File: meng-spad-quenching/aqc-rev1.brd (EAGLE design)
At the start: 127 x 88.9 mm, 137 parts, among them IC1 ADCMP582, IC2 NC7SV74K8X, IC3 LT3032-5, IC4 OPA342, IC5 OPA342, IC6 LTC1711, IC7 DS1100LU-20+, IC8 LT3032-15, IC9 NC7WZ16P6X, J1 VIN_LOGIC, M1 BSS806N, Q1 MMBTH81, Q2 MMBTH81, Q3 MMBTH81, Q4 MMBTH81, Q5 MMBTH81, Q6 MMBTH81, T1 MMBTH10, T2 MMBTH10, T3 MMBTH10, T4 MMBTH10, T5 MMBTH10, T6 MMBTH10, T7 MMBTH10, U1 SN65EPT21DGK, U2 TPS78233DDCT, U3 SN65EPT22DGK, X1 CONN_SPAD, X2 CONN_PHOTON_COUNTER, X3 CONN_FORCE_QUENCH, X4 CONN_VREF_ONE_SHOT_EXT, X5 CONN_VREF_DIAMOND_IBIAS_EXT, X6 CONN_VREF_CASCODE_IBIAS_EXT

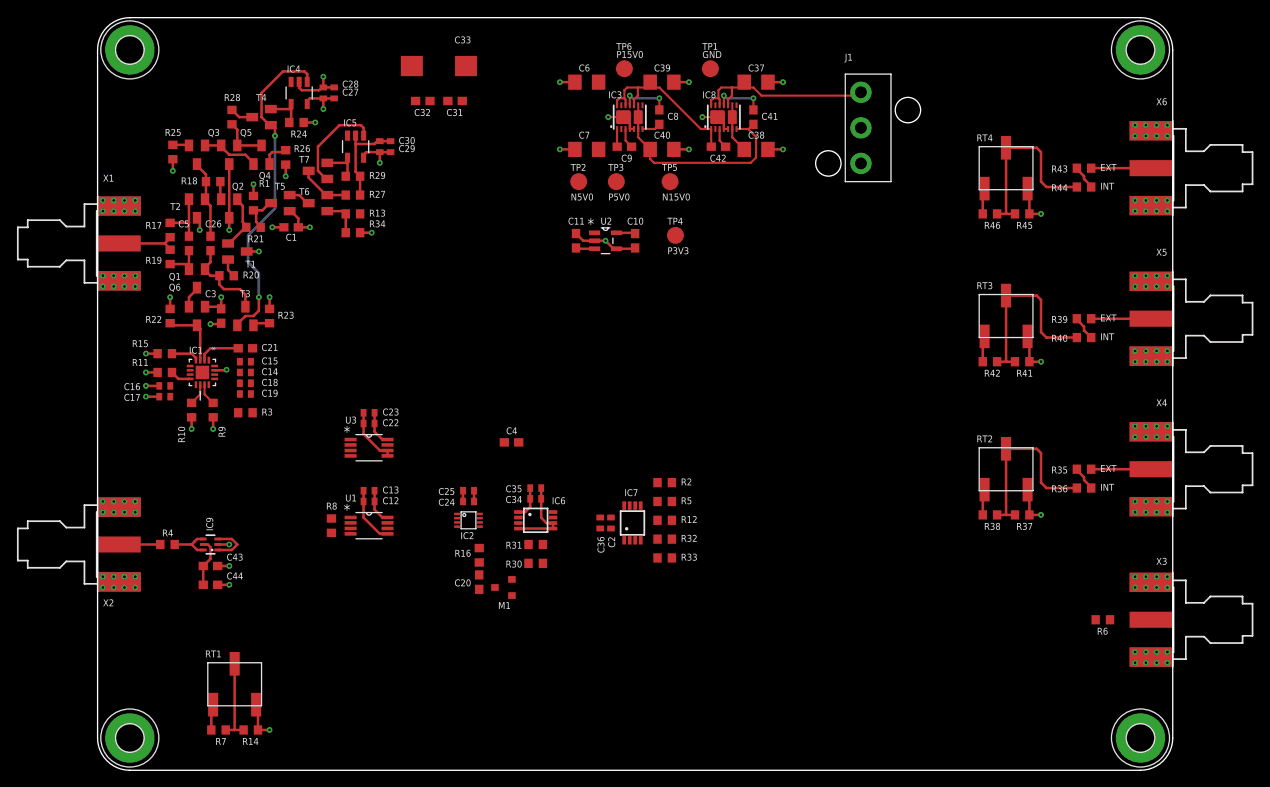
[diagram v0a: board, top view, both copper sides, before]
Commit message: More layout, switched delay line to be driven from line driver
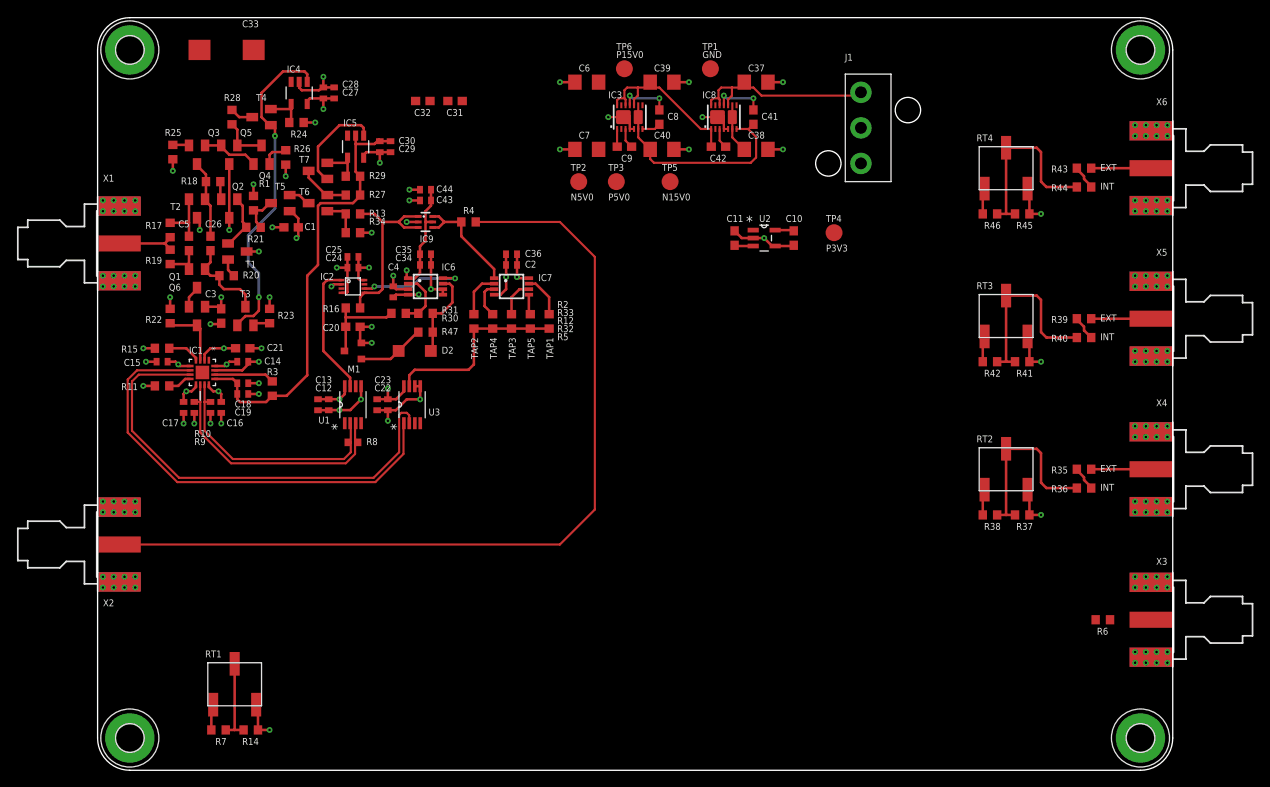
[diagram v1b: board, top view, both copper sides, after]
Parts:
- added D2: SD101BW-TP, diode:SOD123
- added R47: 49R9, rcl:R0603
- C4, C43, C44: device rcl:C0603 -> rcl:C0402
- R10, R8, R9: device rcl:R0603 -> rcl:R0402
- moved C44 53.1 mm to (38.7, 68.6), turned to 180 degrees
- moved R4 52.1 mm to (43.8, 64.8), turned to 180 degrees
- moved C43 50.1 mm to (38.7, 67.3), turned to 180 degrees
- moved IC9 45.8 mm to (38.7, 64.8), turned to 270 degrees
- moved R30 33.7 mm to (35.6, 54.0), turned to 180 degrees
- moved C20 33.7 mm to (30.2, 52.4), turned to 0 degrees
- moved C36 33.4 mm to (48.9, 61.0), turned to 180 degrees
- moved M1 33.1 mm to (30.2, 49.5)
- moved R16 32.8 mm to (30.2, 54.6), turned to 0 degrees
- moved R32 32.8 mm to (46.7, 53.0), turned to 90 degrees
- moved C2 32.7 mm to (48.9, 59.7), turned to 180 degrees
- moved R33 32.1 mm to (51.1, 53.0), turned to 90 degrees
- moved IC7 31.4 mm to (48.9, 57.1), turned to 270 degrees
- moved R5 31.0 mm to (44.5, 53.0), turned to 90 degrees
- moved IC2 30.8 mm to (30.2, 57.1)
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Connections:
- new net N$36: D2.C, M1.1, R47.2
- net LOGIC_QUENCH: no longer IC7.1
- net N$37: now also IC7.1
- net ONE_SHOT_CLR: now also D2.A, R47.1; no longer M1.1
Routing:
- net N$2: track 4.84 -> 103.5 mm
- net PP_P3V3: track 27.6 -> 92.6 mm, vias 0 -> 8
- net COMP_LE_P: track 0.00 -> 54.9 mm
- net COMP_LE_N: track 0.00 -> 54.1 mm
- net PP_N5V0: track 13.9 -> 54.5 mm
- net PP_P5V0: track 22.6 -> 58.8 mm, vias 3 -> 5
- net COMP_Q_N: track 2.57 -> 30.7 mm
- net COMP_Q_P: track 2.57 -> 29.0 mm
- net GND: track 132.9 -> 158.9 mm, vias 128 -> 142
- net BLANKING_LATCH_EN: track 0.00 -> 22.6 mm
- net LOGIC_QUENCH: track 5.19 -> 22.4 mm
- net HOLDOFF_TRIG: track 0.00 -> 15.7 mm
- net !ONE_SHOT_CLR: track 0.00 -> 12.7 mm, vias 0 -> 2
- net ONE_SHOT_CAP: track 0.00 -> 10.7 mm
- net ONE_SHOT_CLR: track 0.00 -> 10.6 mm
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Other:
- board text added: "TAP1"
- board text added: "TAP2"
- board text added: "TAP3"
- board text added: "TAP4"
- board text added: "TAP5"

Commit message: More routing, 21 airwires left!
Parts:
- moved R6 98.7 mm to (30.2, 61.3)
- moved R14 42.2 mm to (50.8, 31.4)
- moved R7 42.2 mm to (47.0, 31.4)
- moved RT1 42.2 mm to (48.9, 36.8)
- moved TP4 42.1 mm to (50.8, 85.1)
- moved C31 35.3 mm to (8.57, 68.3), turned to 270 degrees
- moved C32 32.3 mm to (6.67, 73.0), turned to 90 degrees
- moved TP5 15.6 mm to (66.0, 85.1)
- moved TP2 15.6 mm to (55.9, 85.1)
- moved TP3 15.6 mm to (61.0, 85.1)
- moved TP6 9.16 mm to (71.1, 85.1)
- moved TP1 4.41 mm to (76.2, 85.1)
- moved C37 3.84 mm to (79.4, 77.8)
- moved C38 3.84 mm to (79.4, 69.8)
- moved C39 3.84 mm to (68.3, 77.8)
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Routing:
- net PP_P5V0: track 58.8 -> 148.8 mm, vias 5 -> 7
- net VREF_AV_DET: track 14.6 -> 89.2 mm, vias 1 -> 2
- net PP_P3V3: track 92.6 -> 118.1 mm, vias 8 -> 10
- net PP_P15V0: track 28.0 -> 39.9 mm, vias 5 -> 10
- net !FORCE_QUENCH: track 0.00 -> 6.37 mm, vias 0 -> 1
- net GND: track 158.9 -> 163.6 mm, vias 142 -> 147
- net PP_N15V0: track 25.2 -> 27.1 mm, vias 0 -> 1
- net PP_N5V0: track 54.5 -> 56.4 mm, vias 0 -> 1
- net N$37: track 13.5 -> 14.8 mm
- net LOGIC_QUENCH: track 22.4 -> 23.3 mm
- net PP_PVIN: track 23.9 -> 23.3 mm
- added copper zone on layer 1, net GND
- added copper zone on layer 1, net PP_P15V0
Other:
- board text added: "Comp. Trigger Level Adj."
- board text added: "Latch Delay Select"

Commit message: More routing. 10 airwires!
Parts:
- added C45, C46: 10n, rcl:C0402
- moved C40 8.84 mm to (76.5, 73.0), turned to 90 degrees
- moved C39 7.31 mm to (61.0, 77.5)
- moved C37 7.31 mm to (72.1, 77.5)
- moved C7 6.82 mm to (65.4, 73.0), turned to 90 degrees
- moved C6 6.51 mm to (54.9, 73.0), turned to 90 degrees
- moved C42 5.12 mm to (69.8, 69.5)
- moved C9 5.12 mm to (58.7, 69.5)
- moved C38 4.93 mm to (74.6, 68.6)
- moved C41 4.80 mm to (74.3, 73.0)
- moved IC3 4.80 mm to (59.7, 73.0)
- moved IC8 4.80 mm to (70.8, 73.0)
- moved C8 4.80 mm to (63.2, 73.0)
- turned C11 to 270 degrees
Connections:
- net GND: now also C45.2, C46.2
- net VREF_CASCODE_IBIAS: now also C45.1
- net VREF_DIAMOND_IBIAS: now also C46.1
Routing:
- net VREF_DIAMOND_IBIAS: track 2.93 -> 134.3 mm, vias 0 -> 3
- net VREF_CASCODE_IBIAS: track 2.93 -> 110.6 mm, vias 0 -> 3
- net PP_N5V0: track 56.4 -> 102.0 mm, vias 1 -> 2
- net PP_P15V0: track 39.9 -> 73.2 mm, vias 10 -> 11
- net PP_P3V3: track 118.1 -> 141.5 mm, vias 10 -> 11
- net PP_PVIN: track 23.3 -> 0.00 mm
- net PP_P5V0: track 148.8 -> 159.9 mm, vias 7 -> 8
- net GND: track 163.6 -> 168.3 mm, vias 147 -> 150
- net PP_NVIN: track 5.14 -> 6.67 mm
- net PP_N15V0: track 27.1 -> 26.1 mm, vias 1 -> 4
- added copper zone on layer 1, net PP_N15V0
- added copper zone on layer 1, net PP_N5V0
- added copper zone on layer 1, net PP_NVIN
- added copper zone on layer 1, net PP_P5V0
- added copper zone on layer 1, net PP_PVIN

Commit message: Completed first-pass layout
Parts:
- moved C10 15.6 mm to (68.9, 63.8)
- moved U2 15.6 mm to (65.4, 63.8)
- moved C11 15.6 mm to (61.9, 63.8)
- moved C9 0.63 mm to (58.1, 69.5)
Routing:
- net !FORCE_QUENCH: track 6.37 -> 160.1 mm, vias 1 -> 5
- net PP_P5V0: track 159.9 -> 262.2 mm, vias 8 -> 14
- net PP_P3V3: track 141.5 -> 241.0 mm, vias 11 -> 14
- net VREF_ONE_SHOT: track 6.08 -> 104.5 mm, vias 1 -> 2
- net PP_N15V0: track 26.1 -> 48.1 mm, vias 4 -> 6
- net GND: track 168.3 -> 170.9 mm, vias 150 -> 156
- net VREF_AV_DET: track 89.2 -> 90.2 mm
- added copper zone on layer 15, net GND
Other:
- board text added: "VIN+"
- board text added: "VIN-"

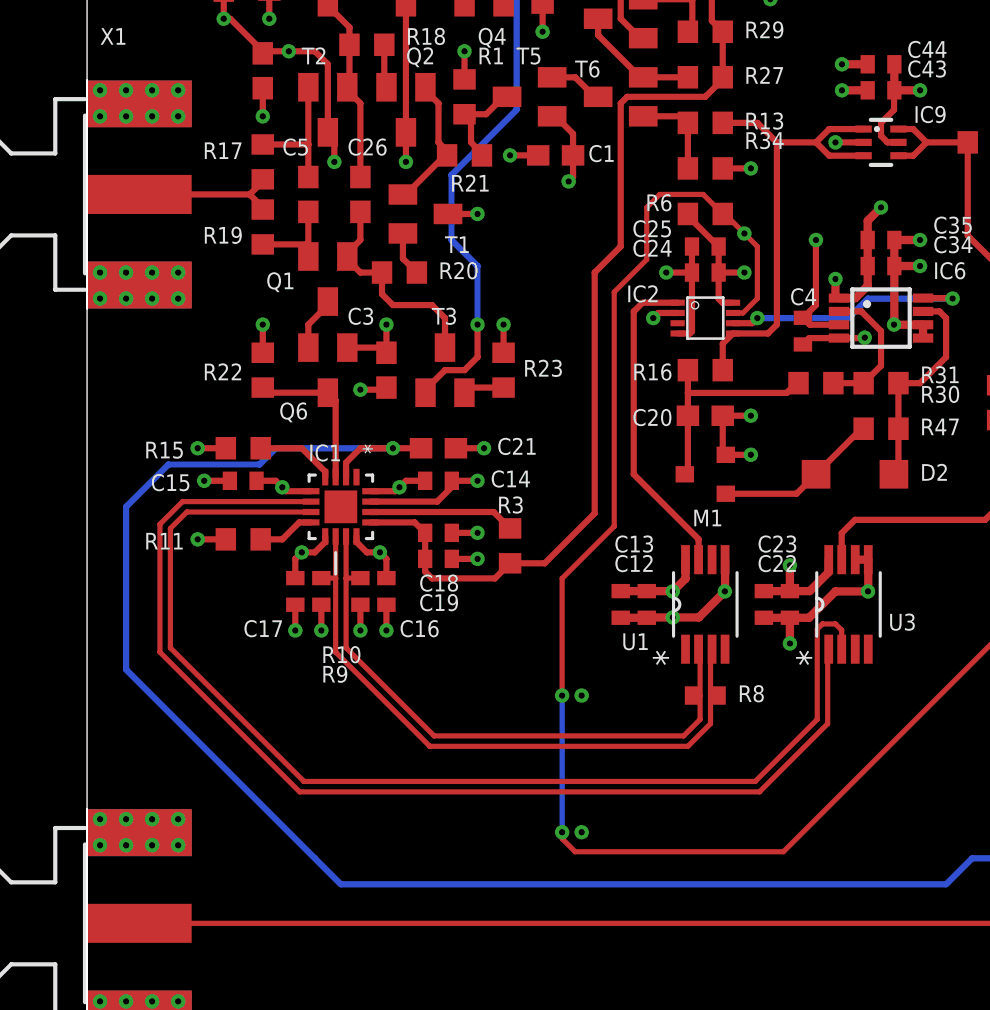
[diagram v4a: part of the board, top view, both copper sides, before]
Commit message: Ran DRC, fixed some overlaps and insufficient clearances
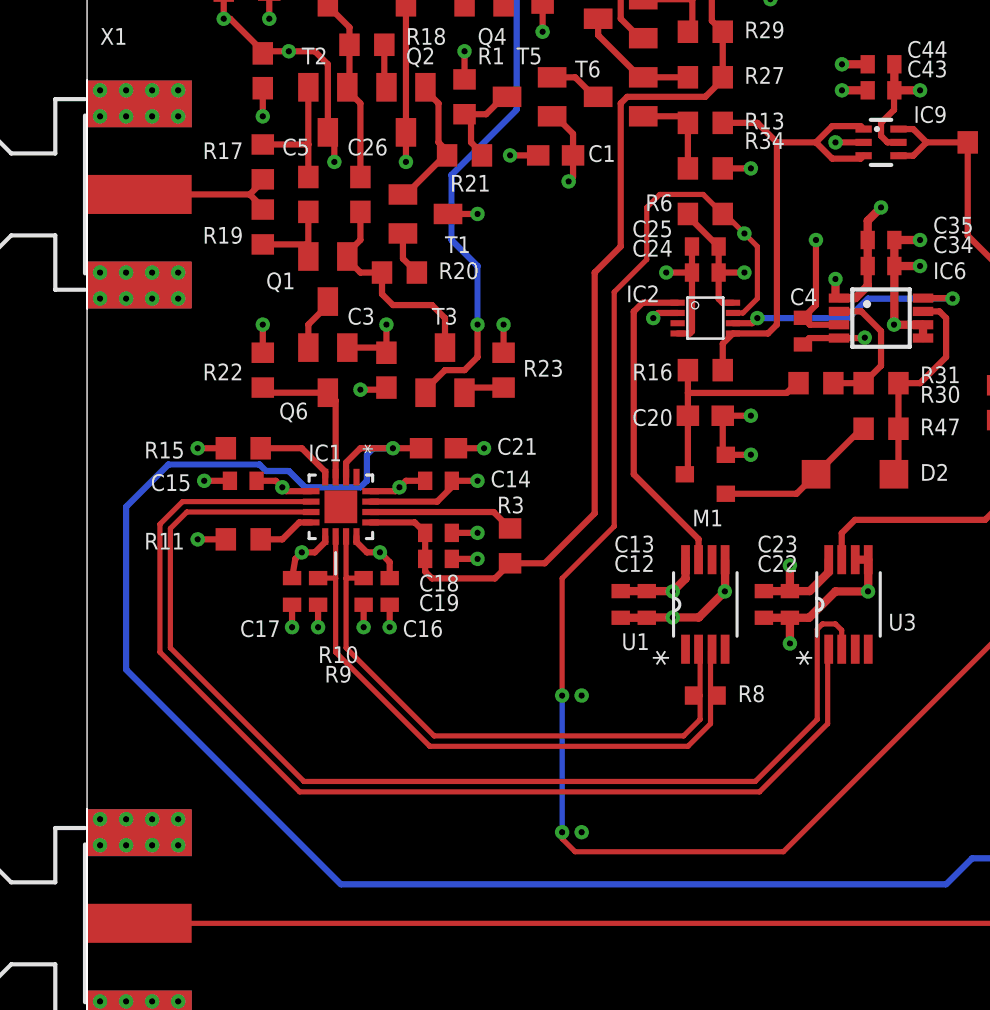
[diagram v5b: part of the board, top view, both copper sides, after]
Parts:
- moved C16 0.16 mm to (14.8, 42.9)
- moved C17 0.16 mm to (10.0, 42.9)
- moved R10 0.16 mm to (11.3, 42.9)
- moved R9 0.16 mm to (13.5, 42.9)
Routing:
- net VREF_AV_DET: track 90.2 -> 91.9 mm
- net GND: track 170.9 -> 170.3 mm

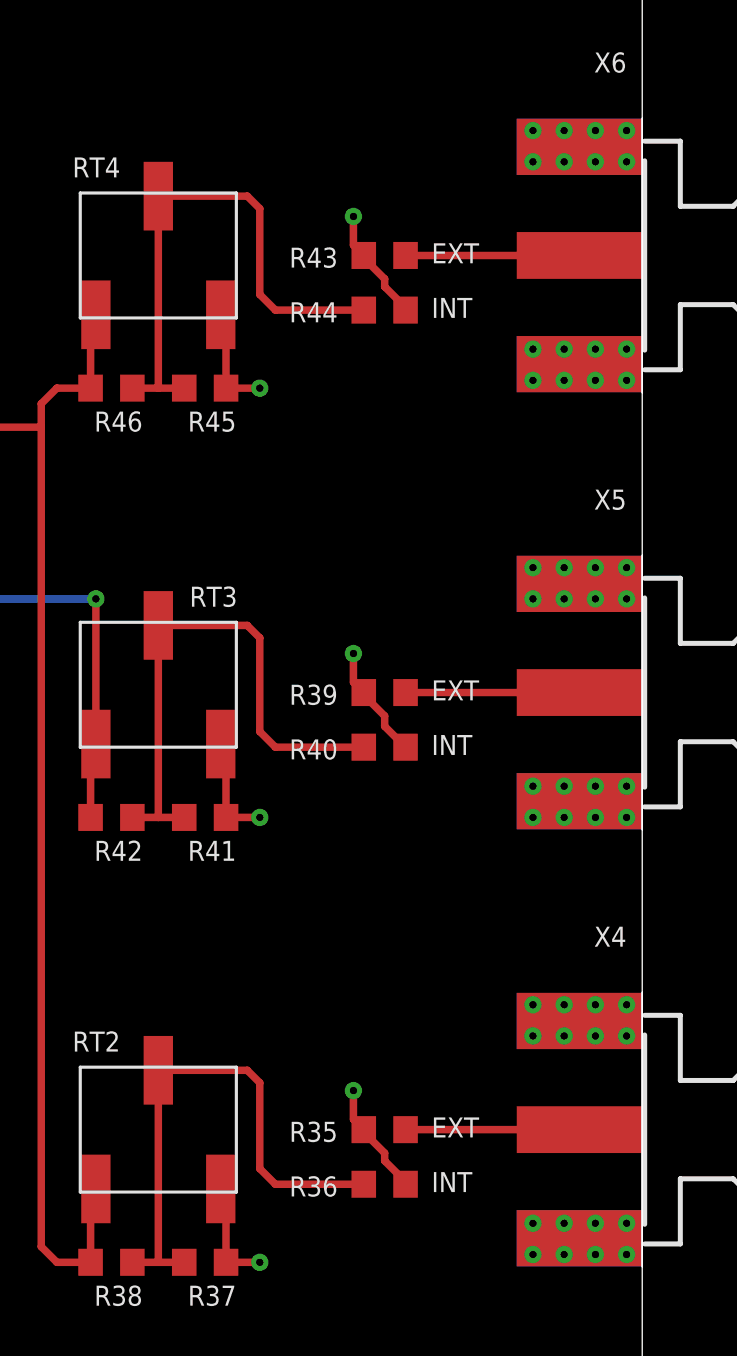
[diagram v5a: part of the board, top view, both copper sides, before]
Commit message: Changed reference voltage 0R jumpers to SMT switches, placed and routed
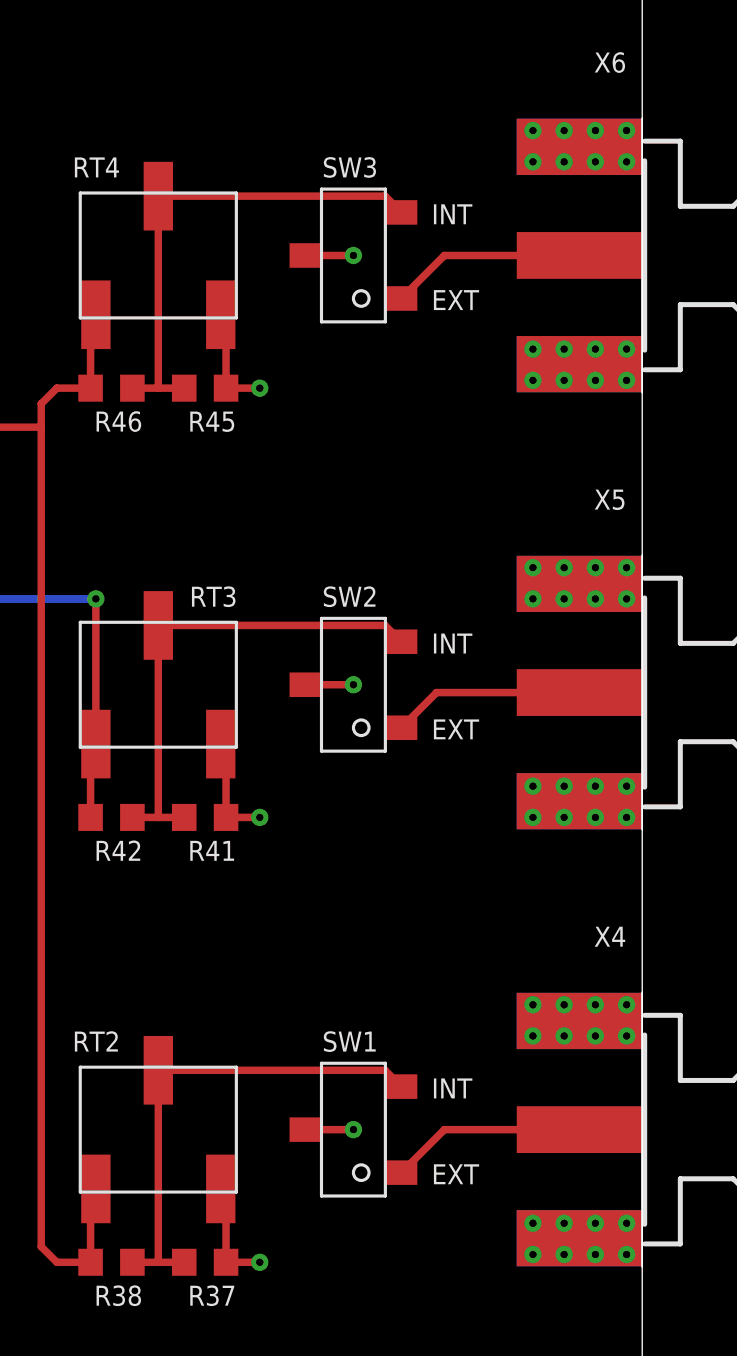
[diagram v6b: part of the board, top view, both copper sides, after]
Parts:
- removed R35, R36, R39, R40, R43, R44: DNP, rcl:R0603
- added SW1, SW2, SW3: CJS-1200TB, meng:CJS-1200TB
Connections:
- net VREF_CASCODE_IBIAS: now also SW3.2; no longer R43.1, R44.1
- net VREF_CASCODE_IBIAS_EXT: now also SW3.1; no longer R43.2
- net VREF_CASCODE_IBIAS_INT: now also SW3.3; no longer R44.2
- net VREF_DIAMOND_IBIAS: now also SW2.2; no longer R39.1, R40.1
- net VREF_DIAMOND_IBIAS_EXT: now also SW2.1; no longer R39.2
- net VREF_DIAMOND_IBIAS_INT: now also SW2.3; no longer R40.2
- net VREF_ONE_SHOT: now also SW1.2; no longer R35.1, R36.1
- net VREF_ONE_SHOT_EXT: now also SW1.1; no longer R35.2
- net VREF_ONE_SHOT_INT: now also SW1.3; no longer R36.2
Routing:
- net VREF_DIAMOND_IBIAS_INT: track 22.6 -> 20.1 mm
- net VREF_CASCODE_IBIAS_INT: track 22.2 -> 20.1 mm
- net VREF_ONE_SHOT_INT: track 22.2 -> 20.1 mm
- net VREF_ONE_SHOT: track 104.5 -> 102.4 mm
- net VREF_DIAMOND_IBIAS: track 134.3 -> 132.8 mm
- net VREF_CASCODE_IBIAS: track 110.7 -> 109.5 mm
- net VREF_ONE_SHOT_EXT: track 7.06 -> 7.96 mm
- net VREF_CASCODE_IBIAS_EXT: track 7.06 -> 7.96 mm
- net VREF_DIAMOND_IBIAS_EXT: track 7.06 -> 7.83 mm
